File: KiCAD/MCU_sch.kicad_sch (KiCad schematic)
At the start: 21 parts, among them IC3 ATSAMS70N20A-AN, Y3 12MHz

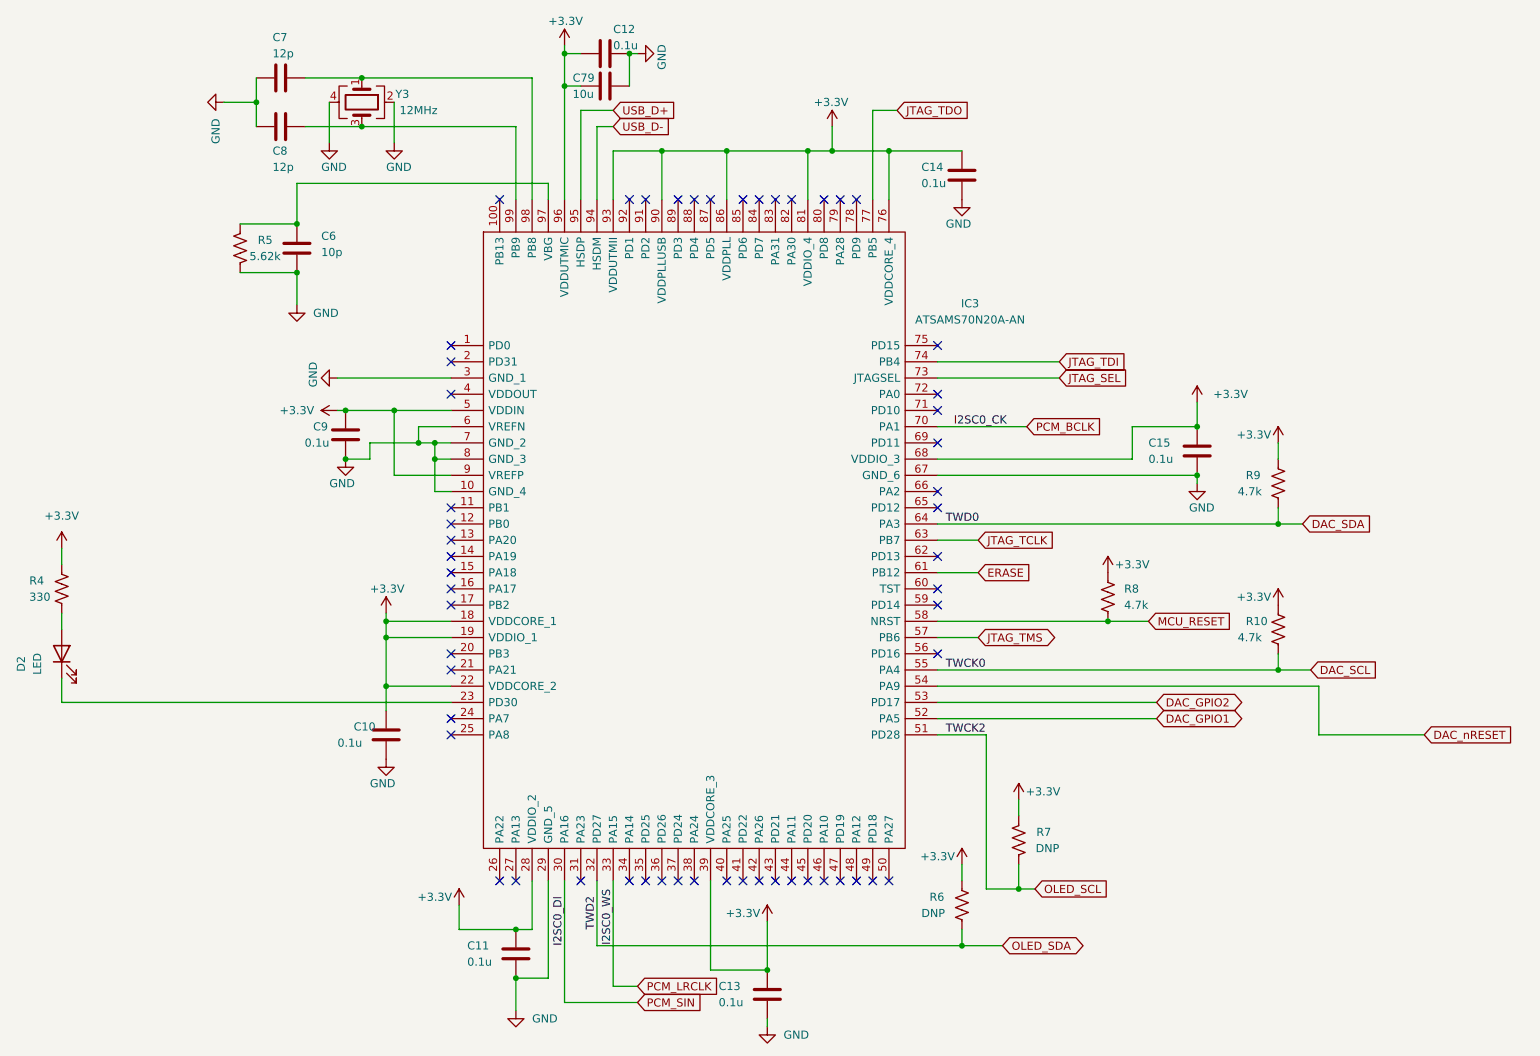
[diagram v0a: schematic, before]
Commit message: Fixing 3.3V being fed to VDDCORE. Swaping 3.3V LDOs to onsemi ones with higher output current
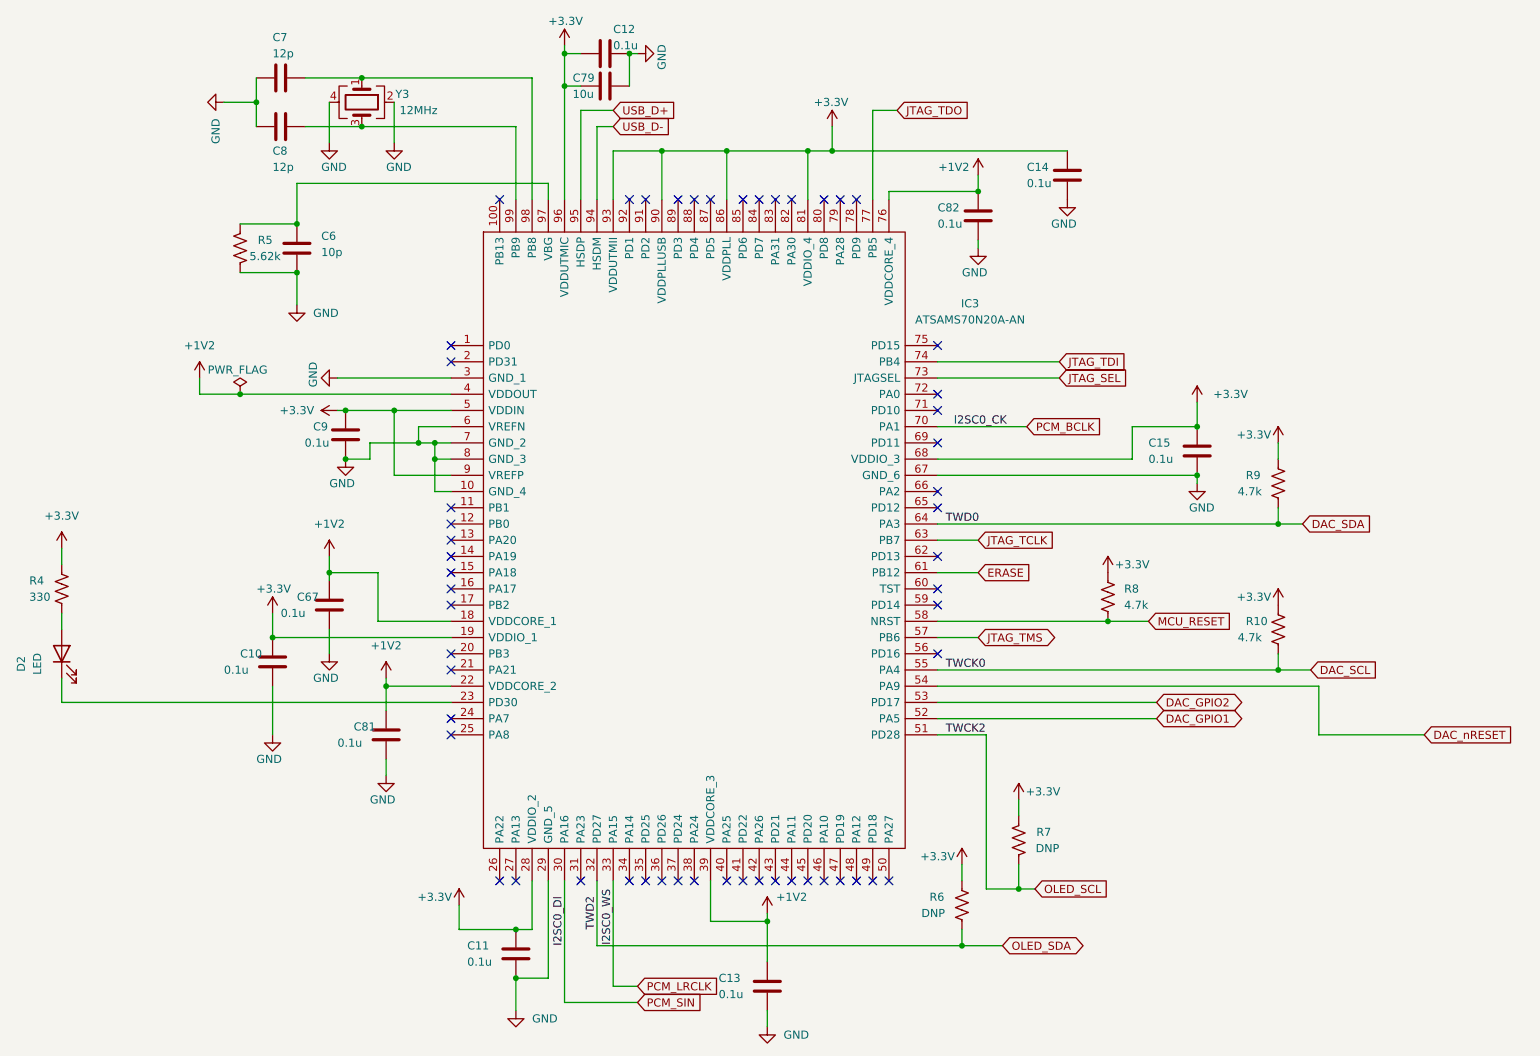
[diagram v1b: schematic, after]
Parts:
- added C67, C81, C82: 0.1u, Capacitor_SMD:C_0805_2012Metric_Pad1.18x1.45mm_HandSolder, symbol Device:C
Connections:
- net +3V3: no longer C13.1, IC3.18 (VDDCORE_1), IC3.22 (VDDCORE_2), IC3.39 (VDDCORE_3), IC3.76 (VDDCORE_4)
- net GND: now also C67.2, C81.2, C82.2
- net +1V2: now reaches IC3.4 (VDDOUT)
- net +1V2: now also C13.1, IC3.18 (VDDCORE_1), IC3.22 (VDDCORE_2), IC3.39 (VDDCORE_3), IC3.76 (VDDCORE_4), C67.1, C81.1, C82.1
- no-connect marks 56 -> 55
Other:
- moved on the sheet: C10, C13, C14

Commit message: Adding stuff for rev 2.0
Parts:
- added C58: 0.1u, Capacitor_SMD:C_0805_2012Metric_Pad1.18x1.45mm_HandSolder, symbol Device:C
- C79: Mouser Part Number 963-LMK212ABJ106KG8T -> 963-TMK212BBJ106KG-T; Part Number LMK212ABJ106KG8T -> TMK212BBJ106KG-T
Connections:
- net +1V2: now also C12.2, C79.2, IC3.86 (VDDPLL), IC3.96 (VDDUTMIC), C58.1
- net +3V3: no longer C12.2, C79.2, IC3.86 (VDDPLL), IC3.96 (VDDUTMIC)
- net GND: now also C58.2
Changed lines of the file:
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@@
   (junction (at 102.87 80.01) (diameter 0) (color 0 0 0 0)
   )
-  (junction (at 167.64 34.29) (diameter 0) (color 0 0 0 0)
+  (junction (at 151.13 25.4) (diameter 0) (color 0 0 0 0)
   )
   (junction (at 196.85 149.86) (diameter 0) (color 0 0 0 0)
@@
   (junction (at 190.5 40.64) (diameter 0) (color 0 0 0 0)
   )
+  (junction (at 204.47 34.29) (diameter 0) (color 0 0 0 0)
+  )
   (junction (at 99.06 74.93) (diameter 0) (color 0 0 0 0)
   )
@@
   )
   (junction (at 91.44 82.55) (diameter 0) (color 0 0 0 0)
-  )
-  (junction (at 151.13 34.29) (diameter 0) (color 0 0 0 0)
   )
   (no_connect (at 107.95 125.73))
@@
     (stroke (width 0) (type default) (color 0 0 0 0))
   )
+  (wire (pts (xy 160.02 25.4) (xy 160.02 27.94))
+    (stroke (width 0) (type default) (color 0 0 0 0))
+  )
   (wire (pts (xy 224.79 73.66) (xy 224.79 77.47))
     (stroke (width 0) (type default) (color 0 0 0 0))
@@
     (stroke (width 0) (type default) (color 0 0 0 0))
   )
-  (wire (pts (xy 151.13 34.29) (xy 151.13 41.91))
-    (stroke (width 0) (type default) (color 0 0 0 0))
-  )
   (wire (pts (xy 80.01 110.49) (xy 107.95 110.49))
     (stroke (width 0) (type default) (color 0 0 0 0))
@@
     (stroke (width 0) (type default) (color 0 0 0 0))
   )
+  (wire (pts (xy 151.13 25.4) (xy 151.13 41.91))
+    (stroke (width 0) (type default) (color 0 0 0 0))
+  )
   (wire (pts (xy 93.98 22.86) (xy 85.09 22.86))
     (stroke (width 0) (type default) (color 0 0 0 0))
@@
     (stroke (width 0) (type default) (color 0 0 0 0))
   )
-  (wire (pts (xy 167.64 30.48) (xy 167.64 34.29))
+  (wire (pts (xy 204.47 29.21) (xy 204.47 34.29))
     (stroke (width 0) (type default) (color 0 0 0 0))
   )
@@
     (stroke (width 0) (type default) (color 0 0 0 0))
   )
+  (wire (pts (xy 158.75 25.4) (xy 160.02 25.4))
+    (stroke (width 0) (type default) (color 0 0 0 0))
+  )
   (wire (pts (xy 184.15 82.55) (xy 214.63 82.55))
     (stroke (width 0) (type default) (color 0 0 0 0))
@@
     (stroke (width 0) (type default) (color 0 0 0 0))
   )
-  (wire (pts (xy 163.83 34.29) (xy 167.64 34.29))
-    (stroke (width 0) (type default) (color 0 0 0 0))
-  )
   (wire (pts (xy 191.77 149.86) (xy 196.85 149.86))
     (stroke (width 0) (type default) (color 0 0 0 0))
@@
     (stroke (width 0) (type default) (color 0 0 0 0))
   )
+  (wire (pts (xy 163.83 34.29) (xy 204.47 34.29))
+    (stroke (width 0) (type default) (color 0 0 0 0))
+  )
   (wire (pts (xy 196.85 146.05) (xy 196.85 149.86))
     (stroke (width 0) (type default) (color 0 0 0 0))
@@
     (stroke (width 0) (type default) (color 0 0 0 0))
   )
-  (wire (pts (xy 151.13 34.29) (xy 163.83 34.29))
+  (wire (pts (xy 140.97 34.29) (xy 163.83 34.29))
     (stroke (width 0) (type default) (color 0 0 0 0))
   )
@@
     (stroke (width 0) (type default) (color 0 0 0 0))
   )
+  (wire (pts (xy 151.13 22.86) (xy 151.13 25.4))
+    (stroke (width 0) (type default) (color 0 0 0 0))
+  )
   (wire (pts (xy 125.73 24.13) (xy 125.73 41.91))
     (stroke (width 0) (type default) (color 0 0 0 0))
@@
     (stroke (width 0) (type default) (color 0 0 0 0))
   )
-  (wire (pts (xy 167.64 34.29) (xy 204.47 34.29))
-    (stroke (width 0) (type default) (color 0 0 0 0))
-  )
   (wire (pts (xy 125.73 24.13) (xy 128.27 24.13))
     (stroke (width 0) (type default) (color 0 0 0 0))
@@
   )
   (wire (pts (xy 68.58 69.85) (xy 68.58 72.39))
-    (stroke (width 0) (type default) (color 0 0 0 0))
-  )
-  (wire (pts (xy 140.97 34.29) (xy 151.13 34.29))
     (stroke (width 0) (type default) (color 0 0 0 0))
   )
@@
     (pin "2")
   )
+  (symbol (lib_id "Device:C") (at 154.94 25.4 90) (unit 1)
+    (in_bom yes) (on_board yes)
+    (property "Reference" "C58" (id 0) (at 154.94 29.21 90)
+      (effects (font (size 1.27 1.27)) (justify left))
+    )
+    (property "Value" "0.1u" (id 1) (at 156.21 31.75 90)
+      (effects (font (size 1.27 1.27)) (justify left))
+    )
+    (property "Footprint" "Capacitor_SMD:C_0805_2012Metric_Pad1.18x1.45mm_HandSolder" (id 2) (at 158.75 24.4348 0)
+      (effects (font (size 1.27 1.27)) hide)
+    )
+    (property "Datasheet" "~" (id 3) (at 154.94 25.4 0)
+      (effects (font (size 1.27 1.27)) hide)
+    )
+    (property "Part Number" "CL21B104KBCNFNC" (id 4) (at 154.94 25.4 0)
+      (effects (font (size 1.27 1.27)) hide)
+    )
+    (property "Mouser Part Number" "187-CL21B104KBCNFNC" (id 5) (at 154.94 25.4 0)
+      (effects (font (size 1.27 1.27)) hide)
+    )
+    (pin "1")
+    (pin "2")
+  )
+  (symbol (lib_id "power:+1V2") (at 151.13 22.86 0) (unit 1)
+    (in_bom yes) (on_board yes)
+    (property "Reference" "#PWR0135" (id 0) (at 151.13 26.67 0)
+      (effects (font (size 1.27 1.27)) hide)
+    )
+    (property "Value" "+1V2" (id 1) (at 147.32 21.59 0))
+    (property "Footprint" "" (id 2) (at 151.13 22.86 0)
+      (effects (font (size 1.27 1.27)) hide)
+    )
+    (property "Datasheet" "" (id 3) (at 151.13 22.86 0)
+      (effects (font (size 1.27 1.27)) hide)
+    )
+    (pin "1")
+  )
   (symbol (lib_id "power:GND") (at 88.9 113.03 0) (unit 1)
     (in_bom yes) (on_board yes)
@@
     (pin "2")
   )
+  (symbol (lib_id "power:GND") (at 160.02 27.94 0) (unit 1)
+    (in_bom yes) (on_board yes)
+    (property "Reference" "#PWR0156" (id 0) (at 160.02 34.29 0)
+      (effects (font (size 1.27 1.27)) hide)
+    )
+    (property "Value" "GND" (id 1) (at 157.48 31.75 0)
+      (effects (font (size 1.27 1.27)) (justify left))
+    )
+    (property "Footprint" "" (id 2) (at 160.02 27.94 0)
+      (effects (font (size 1.27 1.27)) hide)
+    )
+    (property "Datasheet" "" (id 3) (at 160.02 27.94 0)
+      (effects (font (size 1.27 1.27)) hide)
+    )
+    (pin "1")
+  )
   (symbol (lib_id "power:GND") (at 90.17 69.85 270) (unit 1)
     (in_bom yes) (on_board yes)
@@
     (pin "2")
   )
-  (symbol (lib_id "power:+3.3V") (at 125.73 17.78 0) (unit 1)
-    (in_bom yes) (on_board yes)
-    (property "Reference" "#PWR0135" (id 0) (at 125.73 21.59 0)
-      (effects (font (size 1.27 1.27)) hide)
-    )
-    (property "Value" "+3.3V" (id 1) (at 123.19 13.97 0)
-      (effects (font (size 1.27 1.27)) (justify left))
-    )
+  (symbol (lib_id "power:+1V2") (at 125.73 17.78 0) (unit 1)
+    (in_bom yes) (on_board yes)
+    (property "Reference" "#PWR0132" (id 0) (at 125.73 21.59 0)
+      (effects (font (size 1.27 1.27)) hide)
+    )
+    (property "Value" "+1V2" (id 1) (at 121.92 16.51 0))
     (property "Footprint" "" (id 2) (at 125.73 17.78 0)
       (effects (font (size 1.27 1.27)) hide)
@@
       (effects (font (size 1.27 1.27)) hide)
     )
-    (property "Part Number" "LMK212ABJ106KG8T" (id 4) (at 132.08 24.13 90)
-      (effects (font (size 1.27 1.27)) hide)
-    )
-    (property "Mouser Part Number" "963-LMK212ABJ106KG8T" (id 5) (at 132.08 24.13 90)
+    (property "Part Number" "TMK212BBJ106KG-T" (id 4) (at 132.08 24.13 90)
+      (effects (font (size 1.27 1.27)) hide)
+    )
+    (property "Mouser Part Number" "963-TMK212BBJ106KG-T" (id 5) (at 132.08 24.13 90)
       (effects (font (size 1.27 1.27)) hide)
     )
@@
     (pin "99")
   )
-  (symbol (lib_id "power:+3.3V") (at 167.64 30.48 0) (mirror y) (unit 1)
-    (in_bom yes) (on_board yes)
-    (property "Reference" "#PWR0134" (id 0) (at 167.64 34.29 0)
-      (effects (font (size 1.27 1.27)) hide)
-    )
-    (property "Value" "+3.3V" (id 1) (at 170.18 26.67 0)
-      (effects (font (size 1.27 1.27)) (justify left))
-    )
-    (property "Footprint" "" (id 2) (at 167.64 30.48 0)
-      (effects (font (size 1.27 1.27)) hide)
-    )
-    (property "Datasheet" "" (id 3) (at 167.64 30.48 0)
-      (effects (font (size 1.27 1.27)) hide)
-    )
+  (symbol (lib_id "power:+3.3V") (at 204.47 29.21 0) (mirror y) (unit 1)
+    (in_bom yes) (on_board yes)
+    (property "Reference" "#PWR0134" (id 0) (at 204.47 33.02 0)
+      (effects (font (size 1.27 1.27)) hide)
+    )
+    (property "Value" "+3.3V" (id 1) (at 207.01 25.4 0)
+      (effects (font (size 1.27 1.27)) (justify left))
+    )
+    (property "Footprint" "" (id 2) (at 204.47 29.21 0)
+      (effects (font (size 1.27 1.27)) hide)
+    )
+    (property "Datasheet" "" (id 3) (at 204.47 29.21 0)
+      (effects (font (size 1.27 1.27)) hide)
+    )
